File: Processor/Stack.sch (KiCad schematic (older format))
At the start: 26 parts

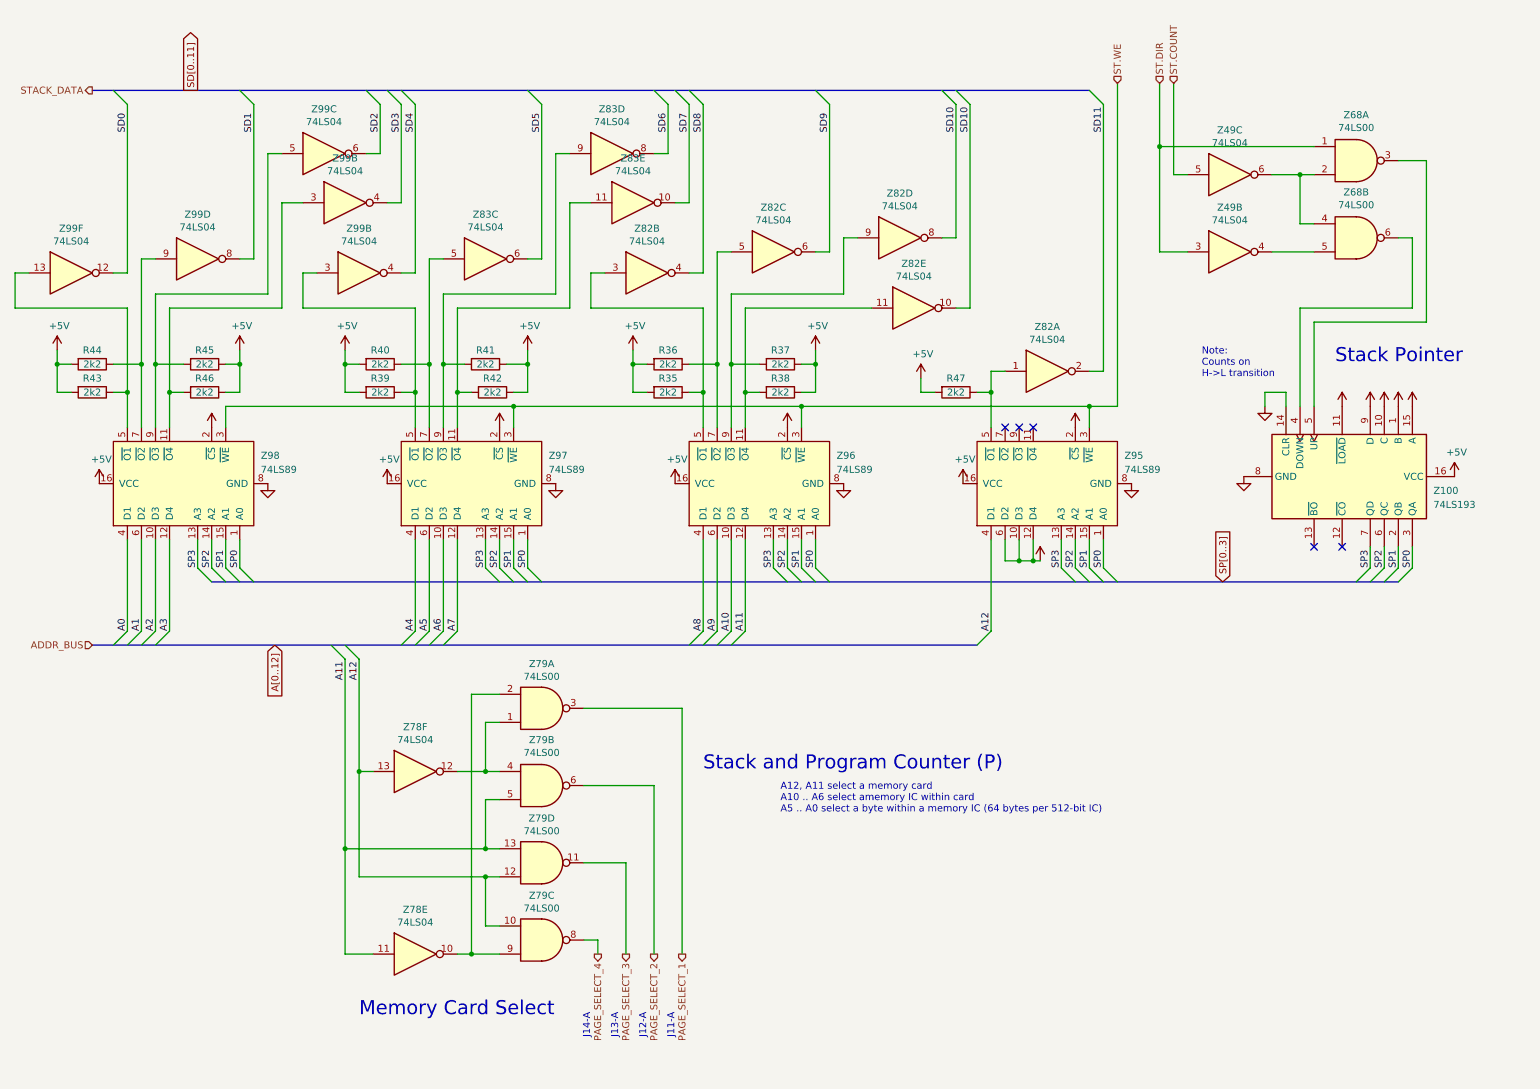
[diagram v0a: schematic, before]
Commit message: Schematics for display & keyboard, adding LEDs to processor PCB
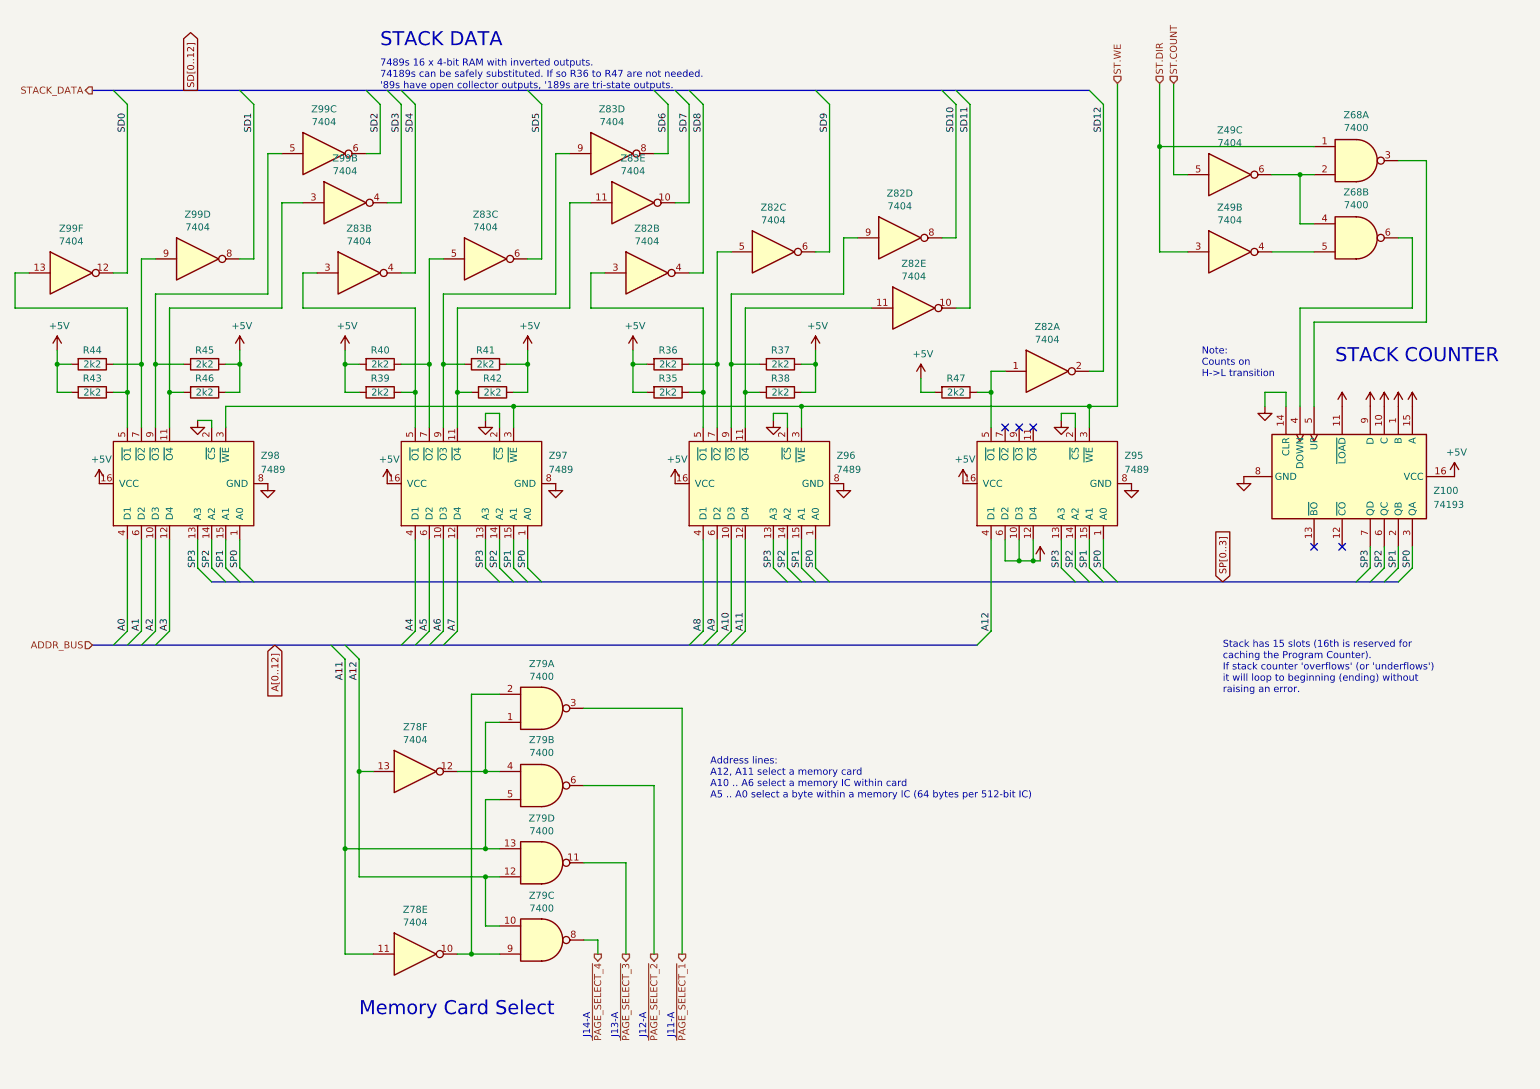
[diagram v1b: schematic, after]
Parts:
- R35, R36, R37, R38, R39, R40, R41, R42, R43, R44, R45, R46, R47: footprint (none) -> Resistor_THT:R_Axial_DIN0207_L6.3mm_D2.5mm_P10.16mm_Horizontal
- Z100: value 74LS193 -> 74193; footprint (none) -> Package_DIP:DIP-16_W7.62mm_Socket
- Z49, Z78, Z82, Z83, Z99: value 74LS04 -> 7404; footprint (none) -> Package_DIP:DIP-14_W7.62mm_Socket
- Z68, Z79: value 74LS00 -> 7400; footprint (none) -> Package_DIP:DIP-14_W7.62mm_Socket
- Z83: renamed from Z99; value 74LS04 -> 7404; footprint (none) -> Package_DIP:DIP-14_W7.62mm_Socket
- Z95, Z96, Z97, Z98: value 74LS89 -> 7489
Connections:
- net +5V: no longer Z95.2 (~CS), Z96.2 (~CS), Z97.2 (~CS), Z98.2 (~CS)
- net GND: now also Z95.2 (~CS), Z96.2 (~CS), Z97.2 (~CS), Z98.2 (~CS)
- net SD10: no longer Z82.10
- net SD11: now also Z82.10; no longer Z82.2
- net PAGE_SELECT_1 renamed ~PAGE_SELECT_1
- net PAGE_SELECT_2 renamed ~PAGE_SELECT_2
- net PAGE_SELECT_3 renamed ~PAGE_SELECT_3
- net PAGE_SELECT_4 renamed ~PAGE_SELECT_4
- new net SD12: Z82.2
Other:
- note added: "7489s 16 x 4-bit RAM with inverted outputs.\n74189s can be safely substituted. If so R36 to R47 are not needed.\n'89s have open collector outputs, '189s are tri-state outputs."
- note added: "Address lines:\nA12, A11 select a memory card\nA10 .. A6 select a memory IC within card\nA5 .. A0 select a byte within a memory IC (64 bytes per 512-bit IC)"
- note added: "STACK COUNTER"
- note added: "STACK DATA"
- note added: "Stack has 15 slots (16th is reserved for \ncaching the Program Counter).\nIf stack counter 'overflows' (or 'underflows')\nit will loop to beginning (ending) without\nraising an error."
- note removed: "A12, A11 select a memory card\nA10 .. A6 select amemory IC within card\nA5 .. A0 select a byte within a memory IC (64 bytes per 512-bit IC)"
- note removed: "Stack Pointer"
- note removed: "Stack and Program Counter (P)"
